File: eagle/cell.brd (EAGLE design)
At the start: 50.3 x 53.5 mm, 11 parts

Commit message: add pcb text
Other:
- board text added: "Harold Cooper"
- board text added: "Heat Seek NYC Cell v0.1"
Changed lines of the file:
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@@
 <hole x="18.796" y="8.509" drill="3.302"/>
 <hole x="31.496" y="44.9834" drill="3.302"/>
+<text x="3.81" y="46.99" size="1.778" layer="21" font="vector" ratio="15">Heat Seek NYC
+Cell v0.1</text>
+<text x="26.67" y="59.69" size="1.778" layer="51" font="vector" ratio="15">Harold Cooper</text>
 </plain>
 <attributes>
@@
 </board>
 </drawing>
+<compatibility>
+<note version="6.3" minversion="6.2.2" severity="warning">
+Since Version 6.2.2 text objects can contain more than one line,
+which will not be processed correctly with this version.
+</note>
+</compatibility>
 </eagle>

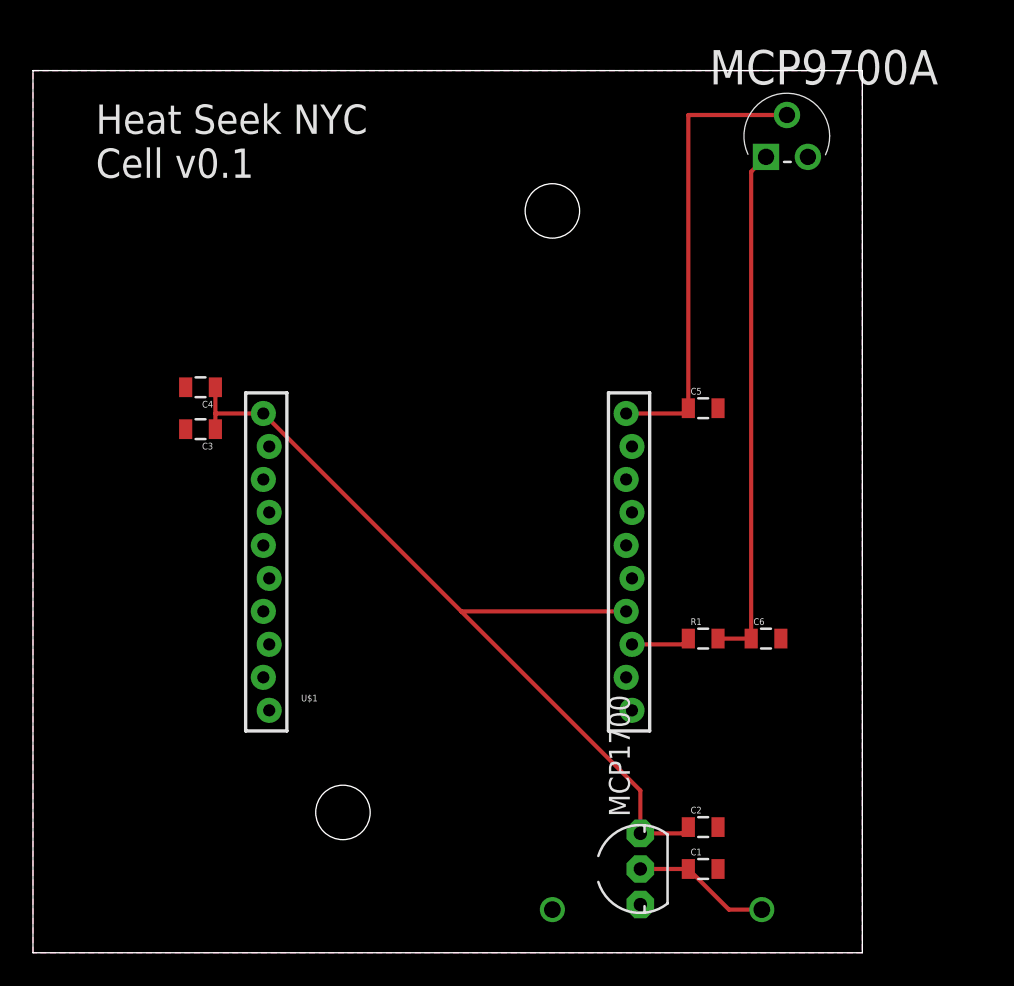
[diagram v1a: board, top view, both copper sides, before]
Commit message: cell v0.1, as ordered from OSH Park on 2014-10-07
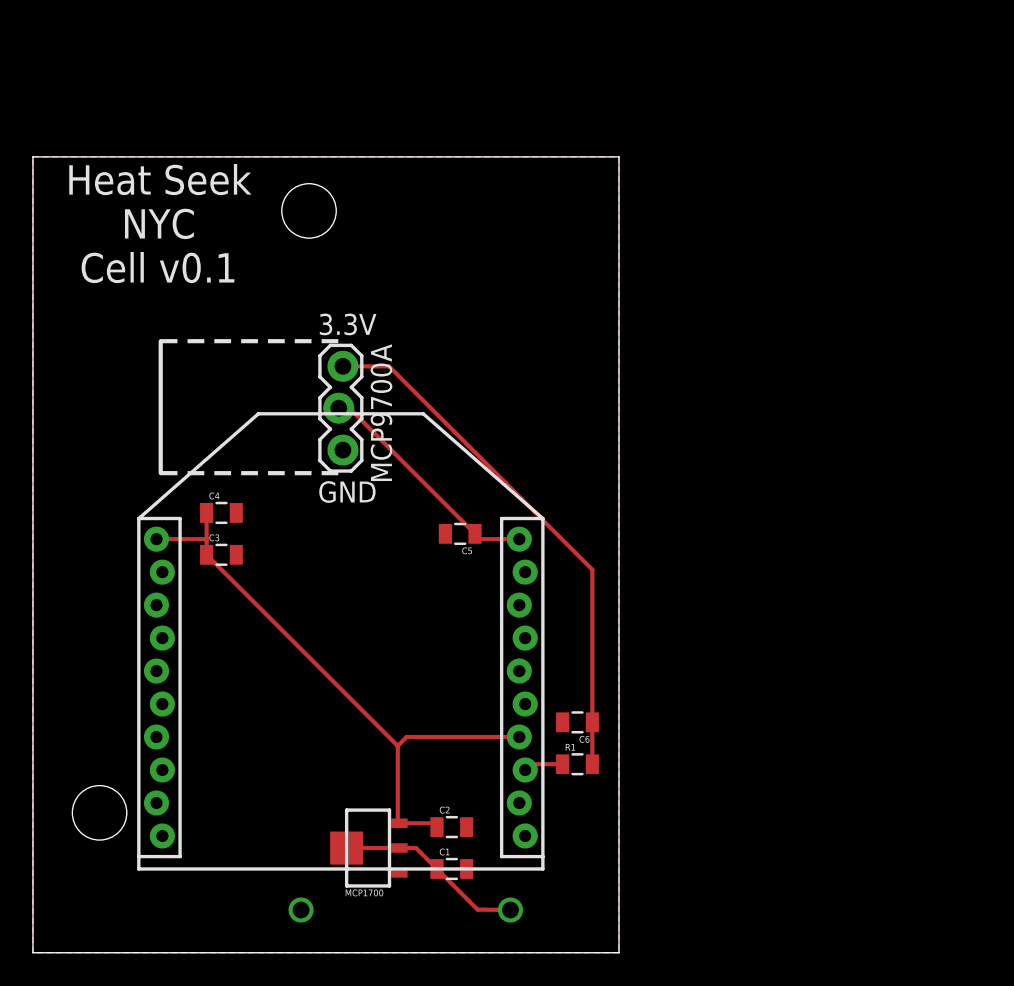
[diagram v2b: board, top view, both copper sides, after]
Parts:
- removed U$1: XBEE-1XBEE-1_LOCK, SparkFun-RF:XBEE-1_LOCK
- added XB24: XBEE-1XBEE-1_LOCK, hrldcpr:XBEE-1_LOCK
- MCP1700: value (none) -> MCP1700; device adafruit:TO92-INLINE -> hrldcpr:SOT-89-3
- MCP9700A: value MCP9700A-E/TO -> (none); device Microchip_By_element14_Batch_1:TO127P254X533-3 -> SparkFun-Connectors:1X03_LOCK
- moved MCP9700A 32.2 mm to (18.7, 35.6), turned to 270 degrees
- moved C5 16.6 mm to (25.9, 25.4), turned to 180 degrees
- moved MCP1700 16.6 mm to (20.3, 6.35)
- moved C1 15.2 mm to (25.4, 5.08)
- moved C2 15.2 mm to (25.4, 7.62)
- moved C6 12.5 mm to (33.0, 14.0), turned to 180 degrees
- moved R1 10.8 mm to (33.0, 11.4)
- moved C3 7.73 mm to (11.4, 24.1), turned to 0 degrees
- moved C4 7.73 mm to (11.4, 26.7), turned to 0 degrees
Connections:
- net 3.3V: now also XB24.1, XB24.14; no longer U$1.1, U$1.14
- net GND: now also XB24.10; no longer U$1.10
- net N$2: now also XB24.13; no longer U$1.13
- net N$3: now also XB24.20; no longer U$1.20
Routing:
- net 3.3V: track 53.4 -> 37.1 mm
- net N$3: track 27.7 -> 14.4 mm
- net N$4: track 0.00 -> 2.54 mm
- net N$2: track 3.56 -> 2.42 mm
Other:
- board size 50.3 x 53.5 mm -> 35.5 x 48.3 mm
- board text added: "3.3V"
- board text added: "GND"
